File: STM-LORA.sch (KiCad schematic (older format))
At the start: 22 parts, among them J1 Batt, J10 CONN_02X07, J11 CONN_02X09, J12 CONN_01X02, J13 CONN_01X02, J14 CONN_01X02, J15 CONN_01X03, J2 Solar, J3 CONN_01X17, J4 CONN_01X03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

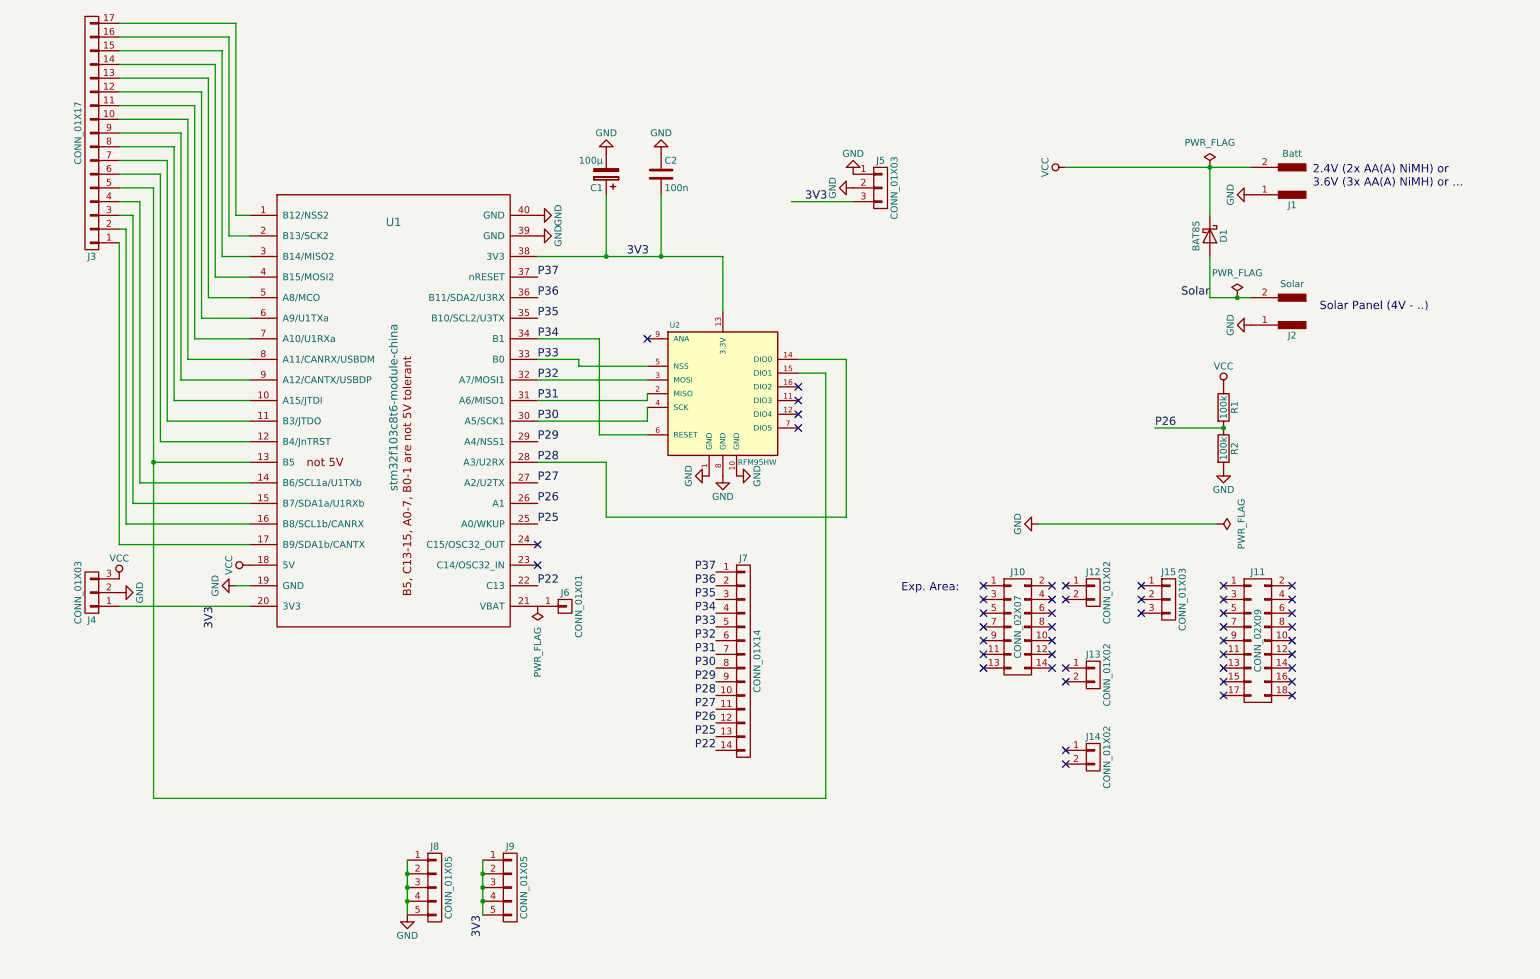
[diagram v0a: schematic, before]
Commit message: Version 0.4 Add antenna hole
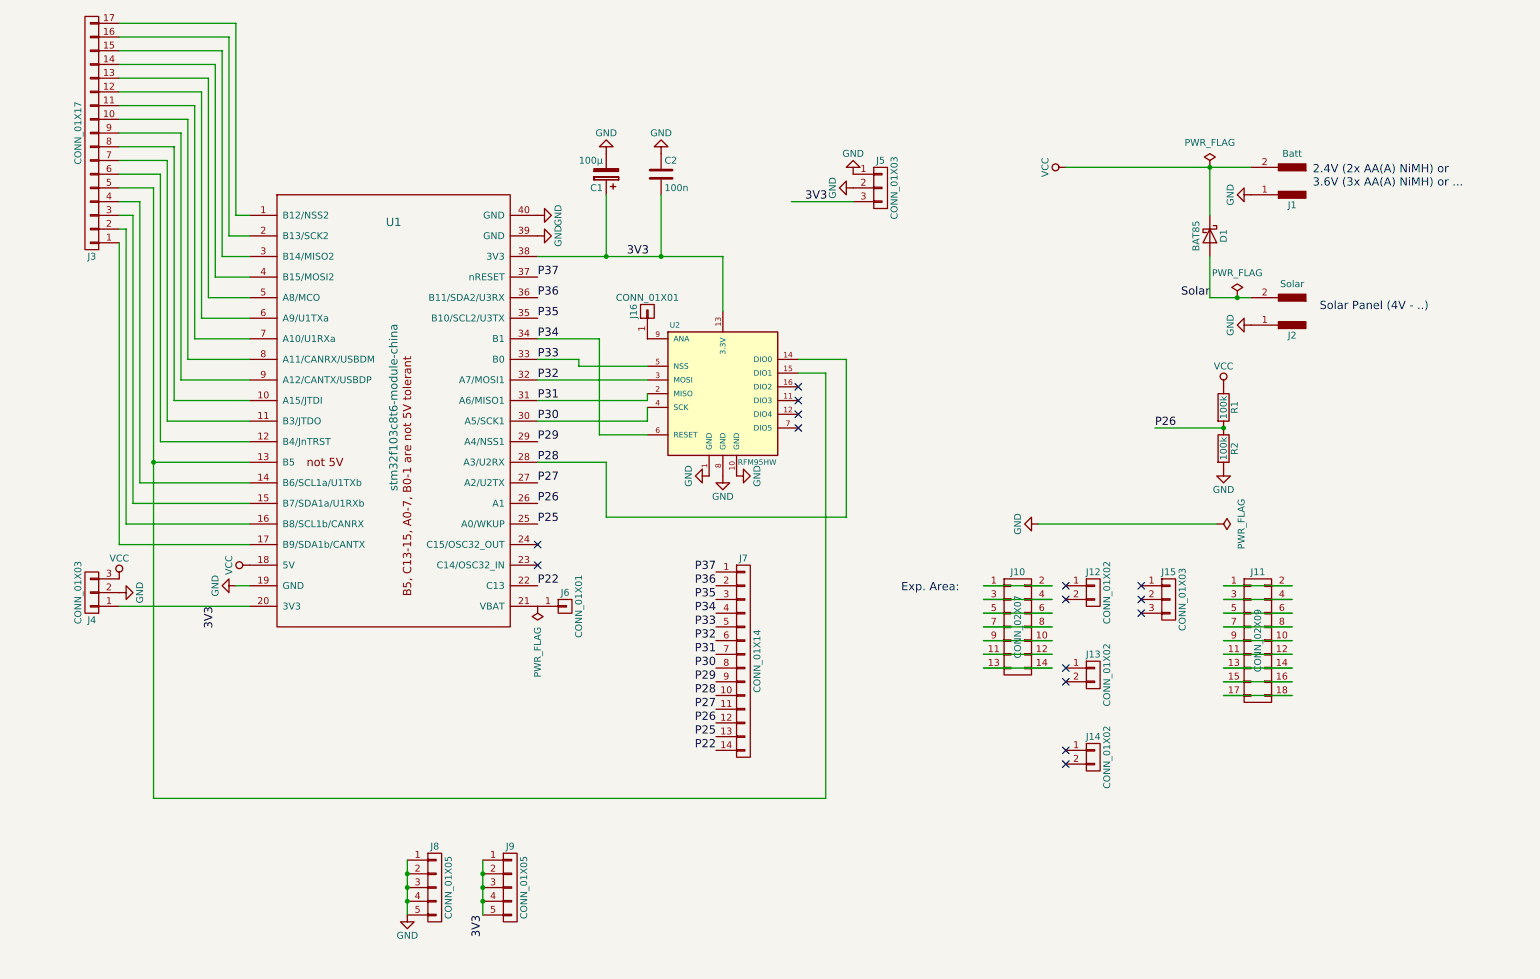
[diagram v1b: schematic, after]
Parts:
- added J16: CONN_01X01, Pin_Headers:Pin_Header_Straight_1x01_Pitch2.54mm, symbol CONN_01X01
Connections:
- net at U2.9 (ANA): now also J16.1 (P1)
- net at J10.1 (P1): now also J10.2 (P2)
- net at J10.10 (P10): now also J10.9 (P9)
- net at J10.11 (P11): now also J10.12 (P12)
- net at J10.13 (P13): now also J10.14 (P14)
- net at J10.3 (P3): now also J10.4 (P4)
- net at J10.5 (P5): now also J10.6 (P6)
- net at J10.7 (P7): now also J10.8 (P8)
- net at J11.1 (P1): now also J11.2 (P2)
- net at J11.10 (P10): now also J11.9 (P9)
- net at J11.11 (P11): now also J11.12 (P12)
- net at J11.13 (P13): now also J11.14 (P14)
- net at J11.15 (P15): now also J11.16 (P16)
- net at J11.17 (P17): now also J11.18 (P18)
- net at J11.3 (P3): now also J11.4 (P4)
- net at J11.5 (P5): now also J11.6 (P6)
- net at J11.7 (P7): now also J11.8 (P8)
- no-connect marks 48 -> 15
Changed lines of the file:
@@
 Sheet 1 1
 Title "STM32 RFM95 Proto Board"
-Date "2017-04-01"
-Rev "0.2"
+Date "2017-06-10"
+Rev "0.3"
 Comp "http://v7f.eu"
 Comment1 ""
@@
 $EndComp
 NoConn ~ 3900 4800
-NoConn ~ 4700 3150
 NoConn ~ 5800 3500
 NoConn ~ 5800 3600
@@
 	6000 3400 6000 6500
 Wire Wire Line
-	1100 6500 6000 6500
-Wire Wire Line
-	1100 2050 1100 6500
+	6000 6500 1100 6500
+Wire Wire Line
+	1100 6500 1100 2050
 Wire Wire Line
 	1100 4050 1800 4050
@@
 	1    0    0    -1
 $EndComp
-NoConn ~ 7150 4950
-NoConn ~ 7150 5050
-NoConn ~ 7150 5150
-NoConn ~ 7150 5250
-NoConn ~ 7150 5350
-NoConn ~ 7150 5450
-NoConn ~ 7150 5550
-NoConn ~ 7650 4950
-NoConn ~ 7650 5050
-NoConn ~ 7650 5150
-NoConn ~ 7650 5250
-NoConn ~ 7650 5350
-NoConn ~ 7650 5450
-NoConn ~ 7650 5550
 NoConn ~ 7750 4950
 NoConn ~ 7750 5050
@@
 NoConn ~ 8300 5050
 NoConn ~ 8300 5150
-NoConn ~ 8900 4950
-NoConn ~ 8900 5050
-NoConn ~ 8900 5150
-NoConn ~ 8900 5250
-NoConn ~ 8900 5350
-NoConn ~ 8900 5450
-NoConn ~ 8900 5550
-NoConn ~ 8900 5650
-NoConn ~ 8900 5750
-NoConn ~ 9400 4950
-NoConn ~ 9400 5050
-NoConn ~ 9400 5150
-NoConn ~ 9400 5250
-NoConn ~ 9400 5350
-NoConn ~ 9400 5450
-NoConn ~ 9400 5550
-NoConn ~ 9400 5650
-NoConn ~ 9400 5750
+$Comp
+L CONN_01X01 J16
+U 1 1 593BCF25
+P 4700 2950
+F 0 "J16" H 4700 3050 50  0000 C CNN
+F 1 "CONN_01X01" V 4800 2950 50  0000 C CNN
+F 2 "Pin_Headers:Pin_Header_Straight_1x01_Pitch2.54mm" H 4700 2950 50  0001 C CNN
+F 3 "" H 4700 2950 50  0001 C CNN
+	1    4700 2950
+	0    -1   -1   0
+$EndComp
+Wire Wire Line
+	8900 4950 9400 4950
+Wire Wire Line
+	8900 5050 9400 5050
+Wire Wire Line
+	9400 5150 8900 5150
+Wire Wire Line
+	8900 5250 9400 5250
+Wire Wire Line
+	9400 5350 8900 5350
+Wire Wire Line
+	8900 5450 9400 5450
+Wire Wire Line
+	9400 5550 8900 5550
+Wire Wire Line
+	8900 5650 9400 5650
+Wire Wire Line
+	8900 5750 9400 5750
+Wire Wire Line
+	7150 4950 7650 4950
+Wire Wire Line
+	7650 5050 7150 5050
+Wire Wire Line
+	7150 5150 7650 5150
+Wire Wire Line
+	7150 5250 7650 5250
+Wire Wire Line
+	7150 5350 7650 5350
+Wire Wire Line
+	7650 5450 7150 5450
+Wire Wire Line
+	7150 5550 7650 5550
 $EndSCHEMATC

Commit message: Update (3D models) for kicad 4.0.7
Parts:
- removed J1: Batt, Pin_Headers:Pin_Header_Straight_1x02_Pitch2.54mm, symbol CONN_01X02_MALE
- removed J10: CONN_02X07, Pin_Headers:Pin_Header_Straight_2x07_Pitch2.54mm, symbol CONN_02X07
- removed J11: CONN_02X09, Pin_Headers:Pin_Header_Straight_2x09_Pitch2.54mm, symbol CONN_02X09
- removed J2: Solar, Pin_Headers:Pin_Header_Straight_1x02_Pitch2.54mm, symbol CONN_01X02_MALE
- added J1, J2: Conn_01x02, Pin_Headers:Pin_Header_Straight_1x02_Pitch2.54mm, symbol Conn_01x02
- added J10: Conn_02x07_Odd_Even, Pin_Headers:Pin_Header_Straight_2x07_Pitch2.54mm, symbol Conn_02x07_Odd_Even
- added J11: Conn_02x09_Odd_Even, Pin_Headers:Pin_Header_Straight_2x09_Pitch2.54mm, symbol Conn_02x09_Odd_Even
- J12, J13, J14: symbol CONN_01X02 -> Conn_01x02
- J15, J4, J5: symbol CONN_01X03 -> Conn_01x03
- J16, J6: symbol CONN_01X01 -> Conn_01x01
- J3: footprint Socket_Strips:Socket_Strip_Straight_1x17_Pitch2.54mm -> Pin_Headers:Pin_Header_Straight_1x17_Pitch2.54mm; symbol CONN_01X17 -> Conn_01x17
- J7: footprint Socket_Strips:Socket_Strip_Straight_1x14_Pitch2.54mm -> Pin_Headers:Pin_Header_Straight_1x14_Pitch2.54mm; symbol CONN_01X14 -> Conn_01x14
- J8, J9: footprint Socket_Strips:Socket_Strip_Straight_1x05_Pitch2.54mm -> Pin_Headers:Pin_Header_Straight_1x05_Pitch2.54mm; symbol CONN_01X05 -> Conn_01x05
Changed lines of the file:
@@
 EESchema Schematic File Version 2
+LIBS:STM-LORA-rescue
 LIBS:power
 LIBS:device
@@
 $EndComp
 $Comp
-L CONN_01X02_MALE J1
-U 1 1 58DFA0FA
-P 9400 2000
-F 0 "J1" H 9400 2175 50  0000 C CNN
-F 1 "Batt" H 9400 1800 50  0000 C CNN
-F 2 "Pin_Headers:Pin_Header_Straight_1x02_Pitch2.54mm" H 9400 2100 50  0001 C CNN
-F 3 "" H 9400 2100 50  0001 C CNN
-	1    9400 2000
-	-1   0    0    1
-$EndComp
-$Comp
 L GND #PWR017
 U 1 1 58DFA43D
-P 9100 2100
-F 0 "#PWR017" H 9100 1850 50  0001 C CNN
-F 1 "GND" H 9100 1950 50  0000 C CNN
-F 2 "" H 9100 2100 50  0001 C CNN
-F 3 "" H 9100 2100 50  0001 C CNN
-	1    9100 2100
+P 9100 2000
+F 0 "#PWR017" H 9100 1750 50  0001 C CNN
+F 1 "GND" H 9100 1850 50  0000 C CNN
+F 2 "" H 9100 2000 50  0001 C CNN
+F 3 "" H 9100 2000 50  0001 C CNN
+	1    9100 2000
 	0    1    1    0
-$EndComp
-$Comp
-L CONN_01X02_MALE J2
-U 1 1 58DFA467
-P 9400 2950
-F 0 "J2" H 9400 3125 50  0000 C CNN
-F 1 "Solar" H 9400 2750 50  0000 C CNN
-F 2 "Pin_Headers:Pin_Header_Straight_1x02_Pitch2.54mm" H 9400 3050 50  0001 C CNN
-F 3 "" H 9400 3050 50  0001 C CNN
-	1    9400 2950
-	-1   0    0    1
 $EndComp
 $Comp
 L GND #PWR018
 U 1 1 58DFA51A
-P 9100 3050
-F 0 "#PWR018" H 9100 2800 50  0001 C CNN
-F 1 "GND" H 9100 2900 50  0000 C CNN
-F 2 "" H 9100 3050 50  0001 C CNN
-F 3 "" H 9100 3050 50  0001 C CNN
-	1    9100 3050
+P 9100 2950
+F 0 "#PWR018" H 9100 2700 50  0001 C CNN
+F 1 "GND" H 9100 2800 50  0000 C CNN
+F 2 "" H 9100 2950 50  0001 C CNN
+F 3 "" H 9100 2950 50  0001 C CNN
+	1    9100 2950
 	0    1    1    0
 $EndComp
 $Comp
-L CONN_01X17 J3
+L Conn_01x17 J3
 U 1 1 58E01D61
 P 650 1650
 F 0 "J3" H 650 2550 50  0000 C CNN
 F 1 "CONN_01X17" V 750 1650 50  0000 C CNN
-F 2 "Socket_Strips:Socket_Strip_Straight_1x17_Pitch2.54mm" H 650 1650 50  0001 C CNN
+F 2 "Pin_Headers:Pin_Header_Straight_1x17_Pitch2.54mm" H 650 1650 50  0001 C CNN
 F 3 "" H 650 1650 50  0001 C CNN
 	1    650  1650
@@
 $EndComp
 $Comp
-L CONN_01X03 J4
+L Conn_01x03 J4
 U 1 1 58E028DC
 P 650 5000
@@
 $EndComp
 $Comp
-L CONN_01X03 J5
+L Conn_01x03 J5
 U 1 1 58E02E8B
 P 6400 2050
@@
 3V3
 $Comp
-L CONN_01X01 J6
+L Conn_01x01 J6
 U 1 1 58E096FD
 P 4100 5100
@@
 $EndComp
 $Comp
-L CONN_01X14 J7
+L Conn_01x14 J7
 U 1 1 58E0990E
-P 5400 5500
-F 0 "J7" H 5400 6250 50  0000 C CNN
-F 1 "CONN_01X14" V 5500 5500 50  0000 C CNN
-F 2 "Socket_Strips:Socket_Strip_Straight_1x14_Pitch2.54mm" H 5400 5500 50  0001 C CNN
-F 3 "" H 5400 5500 50  0001 C CNN
-	1    5400 5500
+P 5400 5450
+F 0 "J7" H 5400 6200 50  0000 C CNN
+F 1 "CONN_01X14" V 5500 5450 50  0000 C CNN
+F 2 "Pin_Headers:Pin_Header_Straight_1x14_Pitch2.54mm" H 5400 5450 50  0001 C CNN
+F 3 "" H 5400 5450 50  0001 C CNN
+	1    5400 5450
 	1    0    0    -1
 $EndComp
@@
 Solar
 $Comp
-L CONN_01X05 J8
+L Conn_01x05 J8
 U 1 1 58E0ADB1
 P 3150 7150
 F 0 "J8" H 3150 7450 50  0000 C CNN
 F 1 "CONN_01X05" V 3250 7150 50  0000 C CNN
-F 2 "Socket_Strips:Socket_Strip_Straight_1x05_Pitch2.54mm" H 3150 7150 50  0001 C CNN
+F 2 "Pin_Headers:Pin_Header_Straight_1x05_Pitch2.54mm" H 3150 7150 50  0001 C CNN
 F 3 "" H 3150 7150 50  0001 C CNN
 	1    3150 7150
@@
 $EndComp
 $Comp
-L CONN_01X05 J9
+L Conn_01x05 J9
 U 1 1 58E0B40A
 P 3700 7150
 F 0 "J9" H 3700 7450 50  0000 C CNN
 F 1 "CONN_01X05" V 3800 7150 50  0000 C CNN
-F 2 "Socket_Strips:Socket_Strip_Straight_1x05_Pitch2.54mm" H 3700 7150 50  0001 C CNN
+F 2 "Pin_Headers:Pin_Header_Straight_1x05_Pitch2.54mm" H 3700 7150 50  0001 C CNN
 F 3 "" H 3700 7150 50  0001 C CNN
 	1    3700 7150
@@
 Exp. Area:
 $Comp
-L CONN_02X07 J10
-U 1 1 58E22FE3
-P 7400 5250
-F 0 "J10" H 7400 5650 50  0000 C CNN
-F 1 "CONN_02X07" V 7400 5250 50  0000 C CNN
-F 2 "Pin_Headers:Pin_Header_Straight_2x07_Pitch2.54mm" H 7400 4050 50  0001 C CNN
-F 3 "" H 7400 4050 50  0001 C CNN
-	1    7400 5250
-	1    0    0    -1
-$EndComp
-$Comp
-L CONN_02X09 J11
-U 1 1 58E2304D
-P 9150 5350
-F 0 "J11" H 9150 5850 50  0000 C CNN
-F 1 "CONN_02X09" V 9150 5350 50  0000 C CNN
-F 2 "Pin_Headers:Pin_Header_Straight_2x09_Pitch2.54mm" H 9150 4150 50  0001 C CNN
-F 3 "" H 9150 4150 50  0001 C CNN
-	1    9150 5350
-	1    0    0    -1
-$EndComp
-$Comp
-L CONN_01X02 J12
+L Conn_01x02 J12
 U 1 1 58E237FE
-P 7950 5000
-F 0 "J12" H 7950 5150 50  0000 C CNN
-F 1 "CONN_01X02" V 8050 5000 50  0000 C CNN
-F 2 "Pin_Headers:Pin_Header_Straight_1x02_Pitch2.54mm" H 7950 5000 50  0001 C CNN
-F 3 "" H 7950 5000 50  0001 C CNN
-	1    7950 5000
-	1    0    0    -1
-$EndComp
-$Comp
-L CONN_01X02 J13
+P 8050 5000
+F 0 "J12" H 8050 5150 50  0000 C CNN
+F 1 "CONN_01X02" V 8150 5000 50  0000 C CNN
+F 2 "Pin_Headers:Pin_Header_Straight_1x02_Pitch2.54mm" H 8050 5000 50  0001 C CNN
+F 3 "" H 8050 5000 50  0001 C CNN
+	1    8050 5000
+	1    0    0    -1
+$EndComp
+$Comp
+L Conn_01x02 J13
 U 1 1 58E23852
-P 7950 5600
-F 0 "J13" H 7950 5750 50  0000 C CNN
-F 1 "CONN_01X02" V 8050 5600 50  0000 C CNN
-F 2 "Pin_Headers:Pin_Header_Straight_1x02_Pitch2.54mm" H 7950 5600 50  0001 C CNN
-F 3 "" H 7950 5600 50  0001 C CNN
-	1    7950 5600
-	1    0    0    -1
-$EndComp
-$Comp
-L CONN_01X02 J14
+P 8050 5600
+F 0 "J13" H 8050 5750 50  0000 C CNN
+F 1 "CONN_01X02" V 8150 5600 50  0000 C CNN
+F 2 "Pin_Headers:Pin_Header_Straight_1x02_Pitch2.54mm" H 8050 5600 50  0001 C CNN
+F 3 "" H 8050 5600 50  0001 C CNN
+	1    8050 5600
+	1    0    0    -1
+$EndComp
+$Comp
+L Conn_01x02 J14
 U 1 1 58E238BA
-P 7950 6200
-F 0 "J14" H 7950 6350 50  0000 C CNN
-F 1 "CONN_01X02" V 8050 6200 50  0000 C CNN
-F 2 "Pin_Headers:Pin_Header_Straight_1x02_Pitch2.54mm" H 7950 6200 50  0001 C CNN
-F 3 "" H 7950 6200 50  0001 C CNN
-	1    7950 6200
-	1    0    0    -1
-$EndComp
-$Comp
-L CONN_01X03 J15
+P 8050 6200
+F 0 "J14" H 8050 6350 50  0000 C CNN
+F 1 "CONN_01X02" V 8150 6200 50  0000 C CNN
+F 2 "Pin_Headers:Pin_Header_Straight_1x02_Pitch2.54mm" H 8050 6200 50  0001 C CNN
+F 3 "" H 8050 6200 50  0001 C CNN
+	1    8050 6200
+	1    0    0    -1
+$EndComp
+$Comp
+L Conn_01x03 J15
 U 1 1 58E239DC
 P 8500 5050
@@
 	1    0    0    -1
 $EndComp
-NoConn ~ 7750 4950
-NoConn ~ 7750 5050
-NoConn ~ 7750 5550
-NoConn ~ 7750 5650
-NoConn ~ 7750 6150
-NoConn ~ 7750 6250
 NoConn ~ 8300 4950
 NoConn ~ 8300 5050
 NoConn ~ 8300 5150
 $Comp
-L CONN_01X01 J16
+L Conn_01x01 J16
 U 1 1 593BCF25
 P 4700 2950
@@
 Wire Wire Line
 	7150 5550 7650 5550
+$Comp
+L Conn_02x07_Odd_Even J10
+U 1 1 59C5163A
+P 7350 5250
+F 0 "J10" H 7400 5650 50  0000 C CNN
+F 1 "Conn_02x07_Odd_Even" H 7400 4850 50  0000 C CNN
+F 2 "Pin_Headers:Pin_Header_Straight_2x07_Pitch2.54mm" H 7350 5250 50  0001 C CNN
+F 3 "" H 7350 5250 50  0001 C CNN
+	1    7350 5250
+	1    0    0    -1
+$EndComp
+$Comp
+L Conn_02x09_Odd_Even J11
+U 1 1 59C517EF
+P 9100 5350
+F 0 "J11" H 9150 5850 50  0000 C CNN
+F 1 "Conn_02x09_Odd_Even" H 9150 4850 50  0000 C CNN
+F 2 "Pin_Headers:Pin_Header_Straight_2x09_Pitch2.54mm" H 9100 5350 50  0001 C CNN
+F 3 "" H 9100 5350 50  0001 C CNN
+	1    9100 5350
+	1    0    0    -1
+$EndComp
+$Comp
+L Conn_01x02 J1
+U 1 1 59C51E67
+P 9300 1900
+F 0 "J1" H 9300 2000 50  0000 C CNN
+F 1 "Conn_01x02" H 9300 1700 50  0000 C CNN
+F 2 "Pin_Headers:Pin_Header_Straight_1x02_Pitch2.54mm" H 9300 1900 50  0001 C CNN
+F 3 "" H 9300 1900 50  0001 C CNN
+	1    9300 1900
+	1    0    0    -1
+$EndComp
+$Comp
+L Conn_01x02 J2
+U 1 1 59C51ED6
+P 9300 2850
+F 0 "J2" H 9300 2950 50  0000 C CNN
+F 1 "Conn_01x02" H 9300 2650 50  0000 C CNN
+F 2 "Pin_Headers:Pin_Header_Straight_1x02_Pitch2.54mm" H 9300 2850 50  0001 C CNN
+F 3 "" H 9300 2850 50  0001 C CNN
+	1    9300 2850
+	1    0    0    -1
+$EndComp
+NoConn ~ 7850 5000
+NoConn ~ 7850 5100
+NoConn ~ 7850 5600
+NoConn ~ 7850 5700
+NoConn ~ 7850 6200
+NoConn ~ 7850 6300
 $EndSCHEMATC
